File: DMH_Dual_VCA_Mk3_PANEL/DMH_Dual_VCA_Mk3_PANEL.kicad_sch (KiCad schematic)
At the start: 23 parts, among them J0 Panel_GND_Solder_Wire_Pad

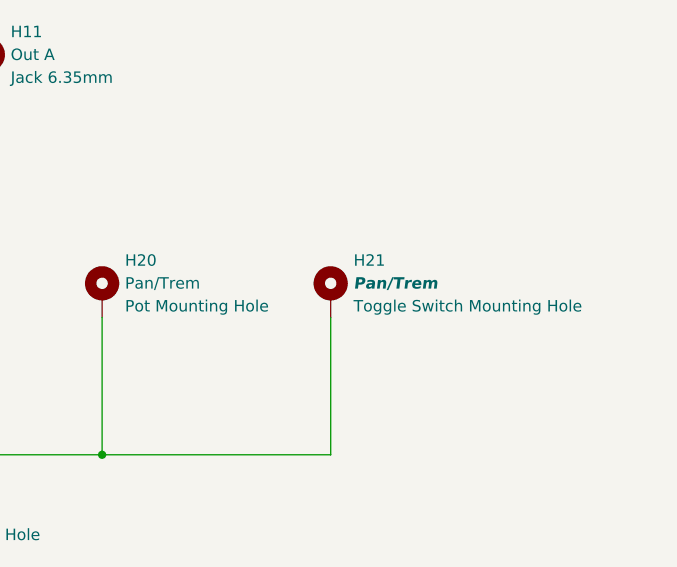
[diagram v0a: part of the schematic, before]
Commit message: Mode switching design in progress
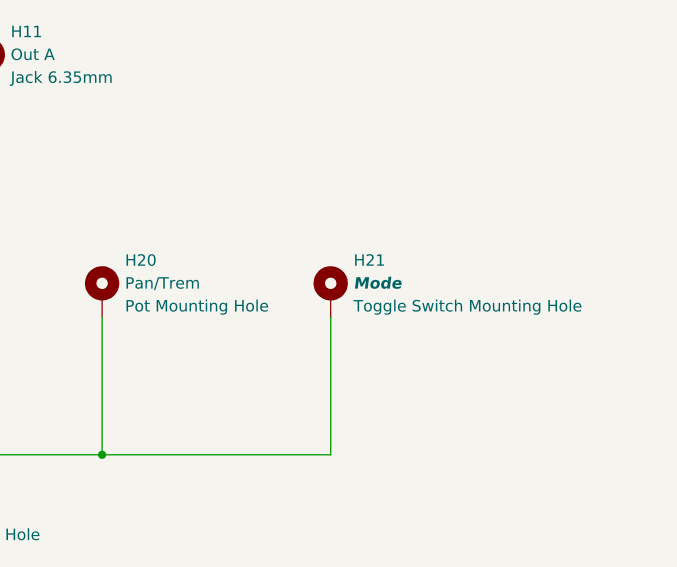
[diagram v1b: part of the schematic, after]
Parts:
- H20: footprint SynthStuff:Pot_Cutout_Tiny_attv_P110KH1 -> SynthStuff:Pot_Cutout_Tiny_attv_RD901F
- H21: value Pan/Trem -> Mode
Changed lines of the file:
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@@
 			)
 		)
-		(property "Value" "Pan/Trem"
+		(property "Value" "Mode"
 			(at 154.94 152.4 0)
 			(effects
@@
 			)
 		)
-		(property "Footprint" "SynthStuff:Pot_Cutout_Tiny_attv_P110KH1"
+		(property "Footprint" "SynthStuff:Pot_Cutout_Tiny_attv_RD901F"
 			(at 127 153.67 0)
 			(effects

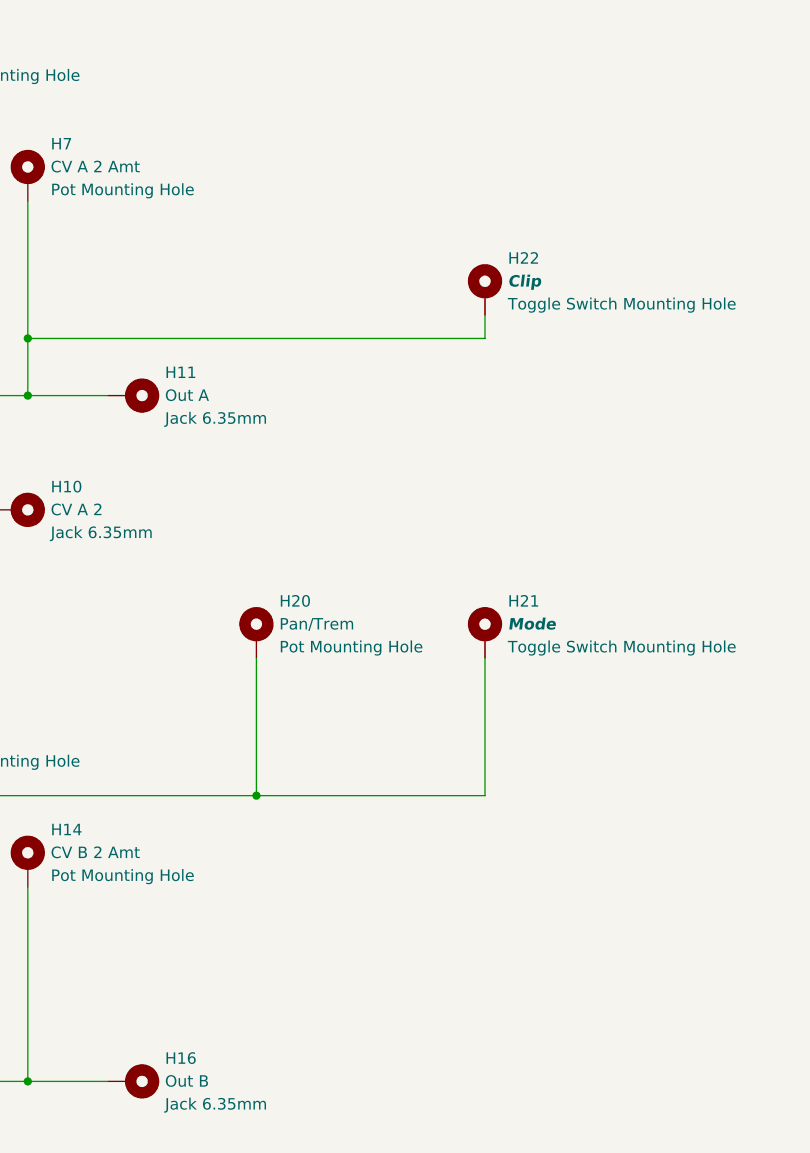
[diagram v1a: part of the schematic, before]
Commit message: Improved clipping indication
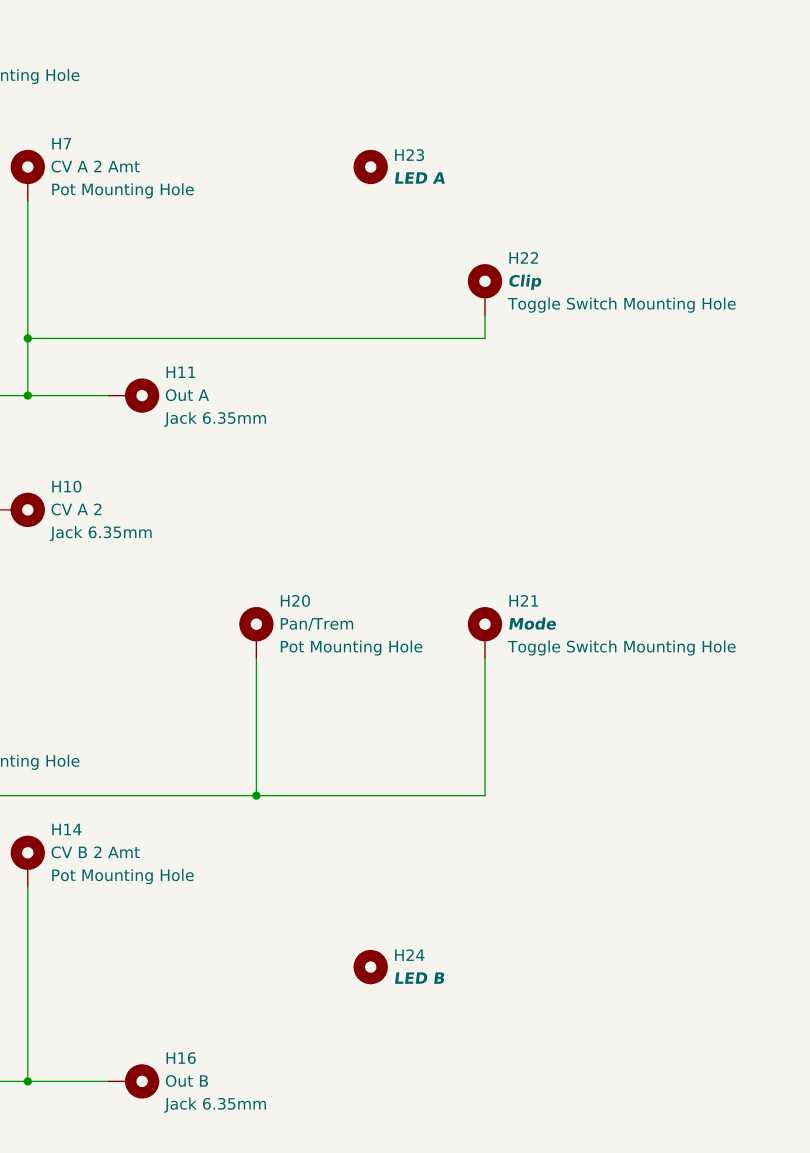
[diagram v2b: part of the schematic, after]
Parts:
- added H23: LED A, SynthStuff:MountingHole_LED_3mm_R, symbol Mechanical:MountingHole
- added H24: LED B, SynthStuff:MountingHole_LED_3mm_R, symbol Mechanical:MountingHole
